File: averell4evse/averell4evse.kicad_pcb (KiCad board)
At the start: 2 copper layers, 91 x 78 mm, 35 parts, among them J1 Conn_01x16, J2 Conn_01x12, J3 Conn_01x04, U1 KT2520K-T, U2 NFCv4, U3 TLC5957RTQ, U4 74AUC1G126, U5 touch_sensor

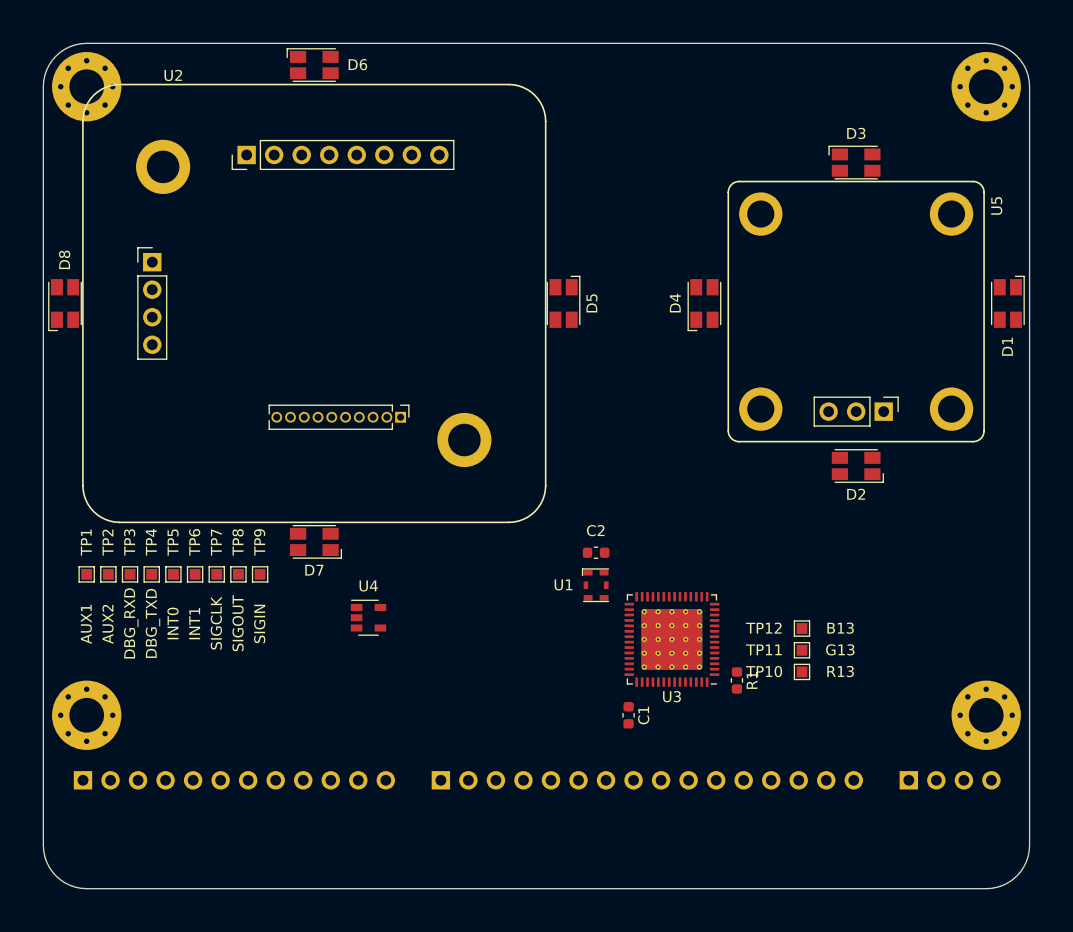
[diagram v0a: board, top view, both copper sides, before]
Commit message: averell/pcb: Routing done
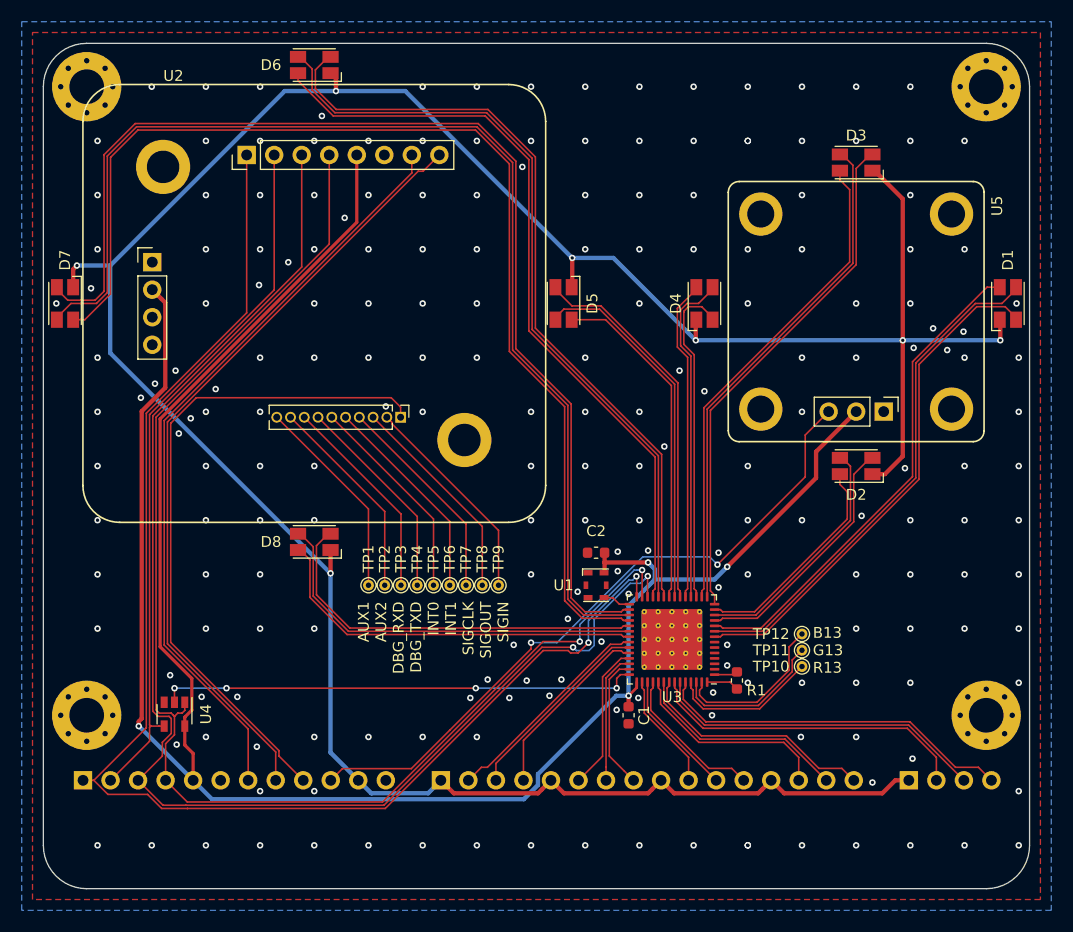
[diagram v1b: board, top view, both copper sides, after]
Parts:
- TP1, TP10, TP11, TP12, TP2, TP3, TP4, TP5, TP6, TP7, TP8, TP9: footprint TestPoint:TestPoint_Pad_1.0x1.0mm -> TestPoint:TestPoint_THTPad_D1.0mm_Drill0.5mm
- moved D7 31.8 mm to (77.0, 75.0), turned to 270 degrees
- moved D8 31.8 mm to (100.0, 97.0), turned to 180 degrees
- moved TP1 26.0 mm to (105.0, 101.0)
- moved TP2 25.5 mm to (106.5, 101.0)
- moved TP3 25.0 mm to (108.0, 101.0)
- moved TP4 24.5 mm to (109.5, 101.0)
- moved TP5 24.0 mm to (111.0, 101.0)
- moved TP6 23.5 mm to (112.5, 101.0)
- moved TP7 23.0 mm to (114.0, 101.0)
- moved TP8 22.5 mm to (115.5, 101.0)
- moved TP9 22.0 mm to (117.0, 101.0)
- moved U4 20.0 mm to (87.1, 112.9), turned to 270 degrees
- moved TP10 0.50 mm to (145.0, 108.5)
- moved TP12 0.50 mm to (145.0, 105.5)
- turned D1 to 90 degrees
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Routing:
- net +5V: track 0.00 -> 258.0 mm, vias 0 -> 7
- net +3V3: track 0.00 -> 209.8 mm, vias 0 -> 4
- net /SCK: track 0.00 -> 127.8 mm, vias 0 -> 2
- net /MOSI: track 0.00 -> 126.3 mm, vias 0 -> 2
- net /NFC_CS: track 0.00 -> 125.0 mm, vias 0 -> 2
- net /G6: track 0.00 -> 107.0 mm
- net /R6: track 0.00 -> 106.9 mm
- net /B6: track 0.00 -> 105.3 mm
- net /~RSTO: track 0.00 -> 72.5 mm
- net /R5: track 0.00 -> 72.0 mm
- net /G5: track 0.00 -> 71.9 mm
- net /IRQ: track 0.00 -> 70.4 mm
- net /B5: track 0.00 -> 70.3 mm
- net /MISO: track 0.00 -> 65.3 mm
- net /TOUCH: track 0.00 -> 63.3 mm, vias 0 -> 2
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- added copper zone on B.Cu, net GND
- added copper zone on F.Cu, net GND
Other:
- board text added: "AUX1 AUX2 DBG_RXD DBG_TXD INT0 INT1 SIGCLK SIGOUT SIGIN"
- board text added: "B13 G13 R13"

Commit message: averell/*: Update LED footprint with custom internal one
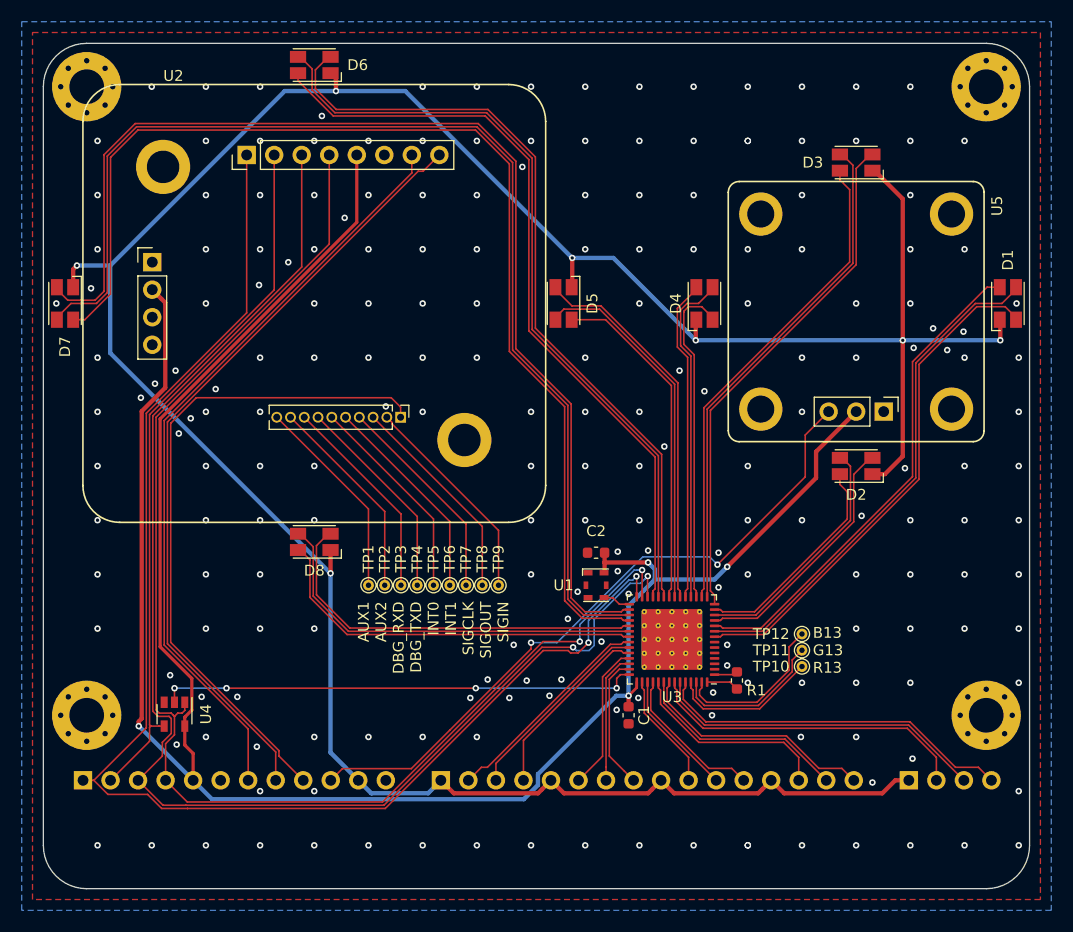
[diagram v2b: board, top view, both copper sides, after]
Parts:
- D1, D2, D3, D4, D5, D6, D7, D8: footprint LED_SMD:LED_Avago_PLCC4_3.2x2.8mm_CW -> ma4evse:LED_Avago_PLCC4_3.2x2.8mm_CW

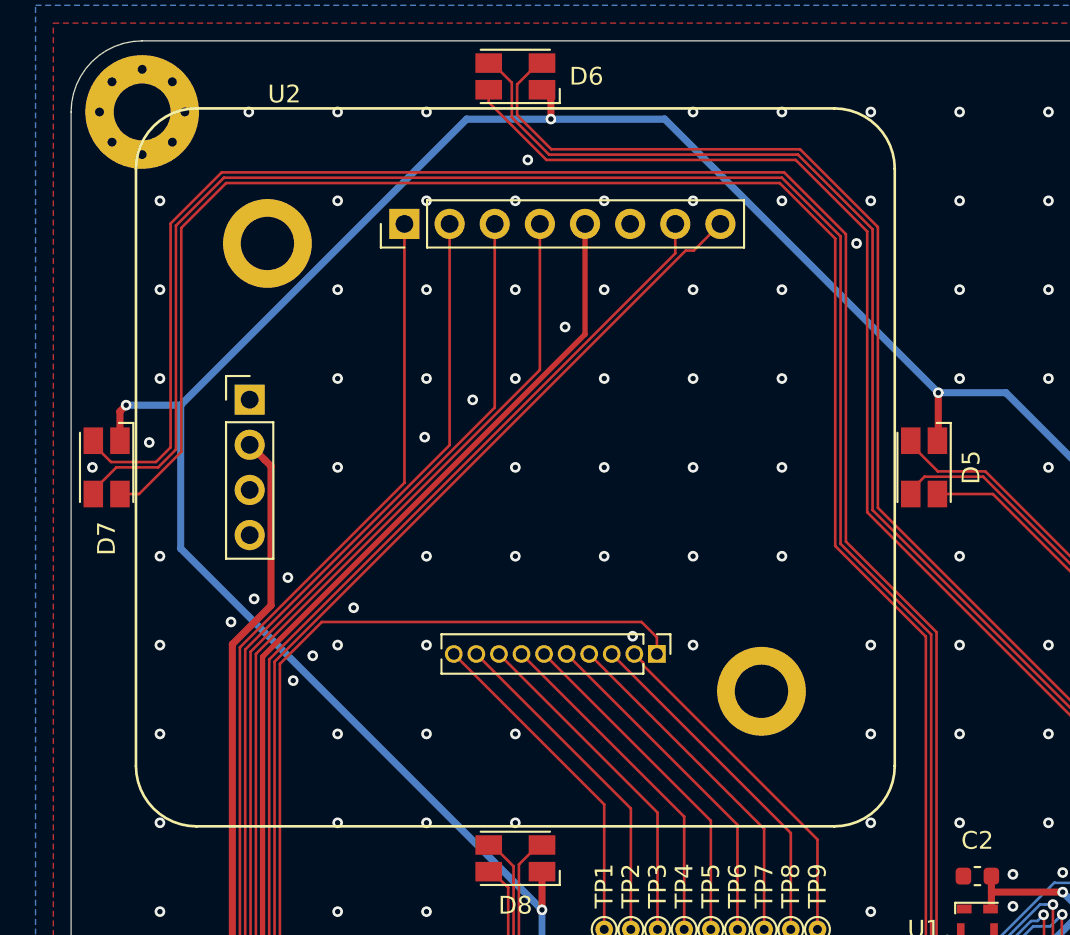
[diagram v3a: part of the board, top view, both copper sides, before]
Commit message: averell/pcb: Add keepout zone under the NFC module
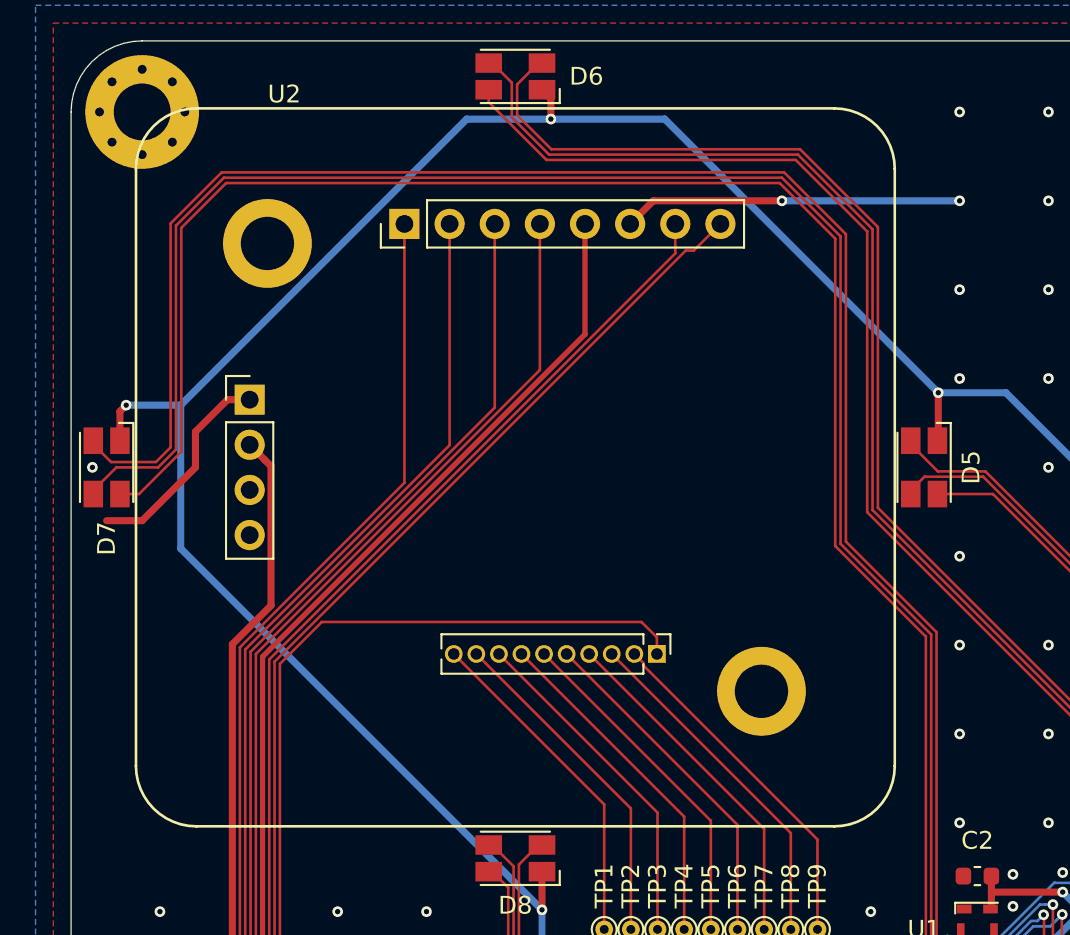
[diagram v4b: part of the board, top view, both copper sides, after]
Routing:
- net GND: track 0.00 -> 31.1 mm, vias 212 -> 146

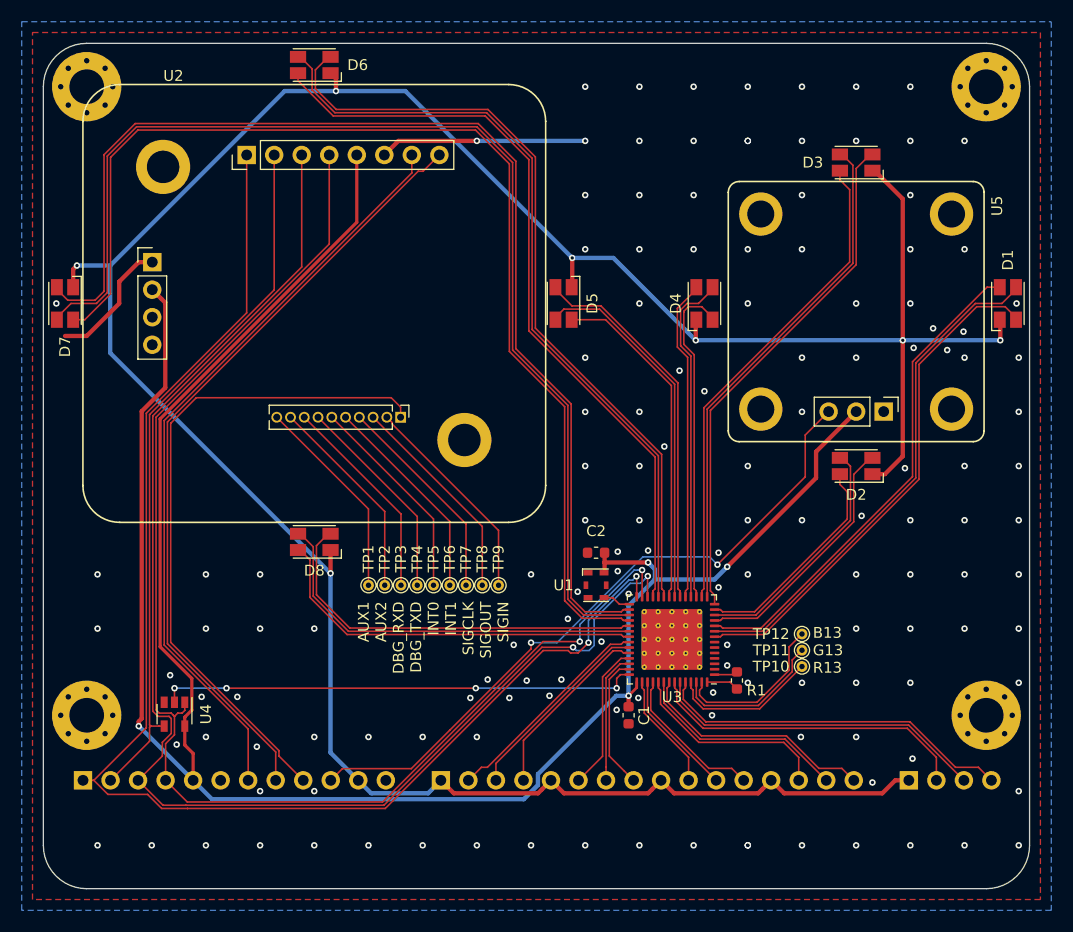
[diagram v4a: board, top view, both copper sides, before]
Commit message: averell/pcb: Re-route with mirror NFCv4 module
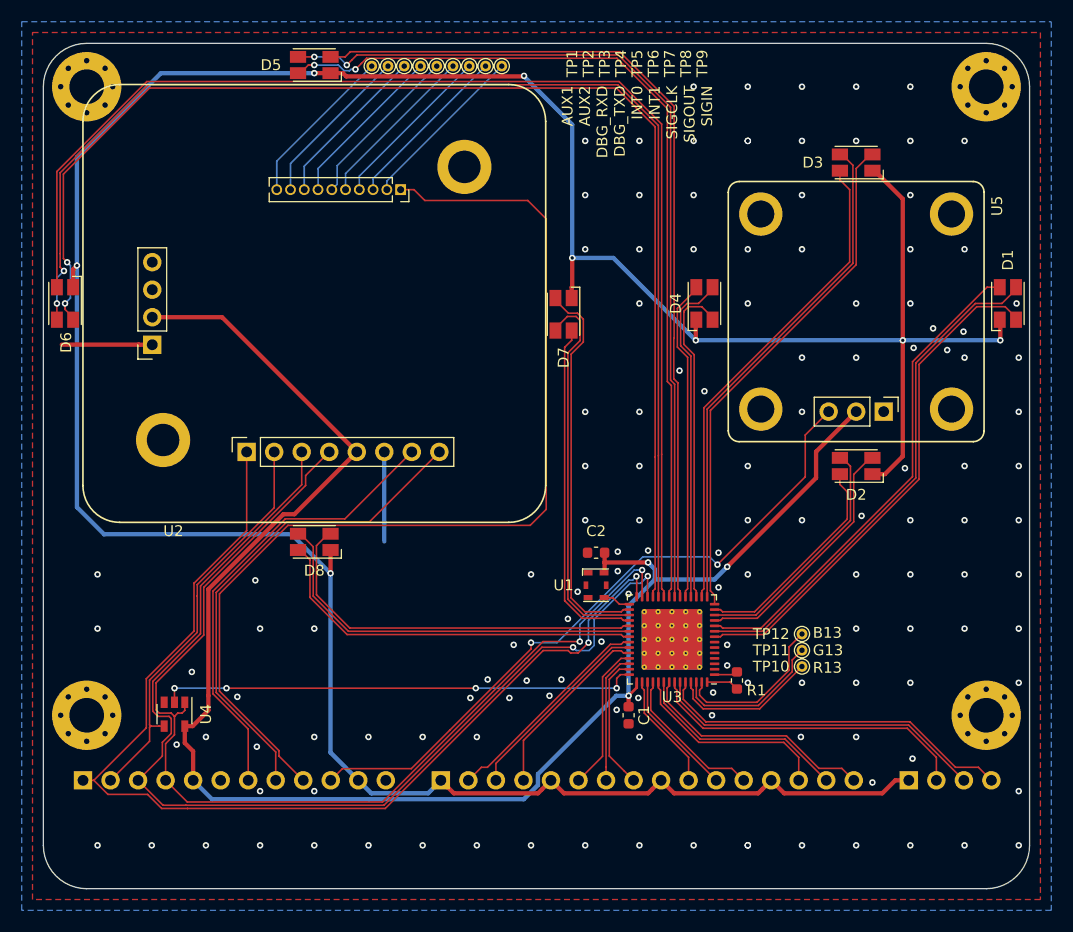
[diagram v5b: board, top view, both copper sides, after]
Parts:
- U2: footprint ma4evse:nfc_v4 -> ma4evse:nfc_v4_mirror
- moved TP1 47.9 mm to (105.3, 53.1)
- moved TP2 47.9 mm to (106.8, 53.1)
- moved TP3 47.9 mm to (108.3, 53.1)
- moved TP4 47.9 mm to (109.8, 53.1)
- moved TP5 47.9 mm to (111.3, 53.1)
- moved TP6 47.9 mm to (112.8, 53.1)
- moved TP7 47.9 mm to (114.3, 53.1)
- moved TP8 47.9 mm to (115.8, 53.1)
- moved TP9 47.9 mm to (117.3, 53.1)
- moved D7 46.0 mm to (123.0, 76.0)
- moved D5 31.8 mm to (100.0, 53.0), turned to 180 degrees
- moved D6 31.8 mm to (77.0, 75.0), turned to 270 degrees
- turned U2 to 180 degrees
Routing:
- net /B6: track 105.3 -> 31.9 mm
- net /G6: track 107.0 -> 35.5 mm
- net /R6: track 106.9 -> 35.7 mm
- net +3V3: track 209.8 -> 156.1 mm, vias 4 -> 3
- net /B4: track 31.3 -> 82.3 mm, vias 0 -> 2
- net /G4: track 34.0 -> 82.4 mm, vias 0 -> 2
- net /B5: track 70.3 -> 117.0 mm, vias 0 -> 2
- net /G5: track 71.9 -> 117.6 mm, vias 0 -> 2
- net /R4: track 34.9 -> 79.5 mm
- net /R5: track 72.0 -> 115.2 mm
- net /~RST: track 61.5 -> 95.1 mm
- net /IRQ: track 70.4 -> 42.5 mm
- net /NFC_CS: track 125.0 -> 97.6 mm
- net /MOSI: track 126.3 -> 98.9 mm
- net /SCK: track 127.8 -> 100.4 mm
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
